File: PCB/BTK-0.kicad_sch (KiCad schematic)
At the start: 94 parts, among them J1 USB_C_Receptacle_USB2.0_16P, J2 BAT+, J3 BAT-, J4 Conn_01x15, J5 Conn_01x15_Socket, SW1 EN, SW10 1,2, SW11 2,2, SW12 3,2, SW13 4,2, SW14 5,2, SW15 6,2, SW16 1,3, SW17 2,3, SW18 3,3, SW19 4,3, SW2 BOOT, SW20 5,3, SW21 6,3, SW22 1,4, SW23 2,4, SW24 3,4, SW25 4,4, SW26 5,4, SW27 6,4, SW28 1,4, SW29 2,4, SW3 RotaryEncoder_Switch_MP, SW30 3,4, SW31 4,4, SW32 5,4, SW33 6,4, SW4 1,1, SW5 2,1, SW6 3,1, SW7 4,1, SW8 5,1, SW9 6,1, U1 NCP1117-3.3_SOT223, U2 NCP1117-3.3_SOT223, U3 USBLC6-2SC6, U4 ESP32-C6-MINI-1, U5 TVS1400DRV

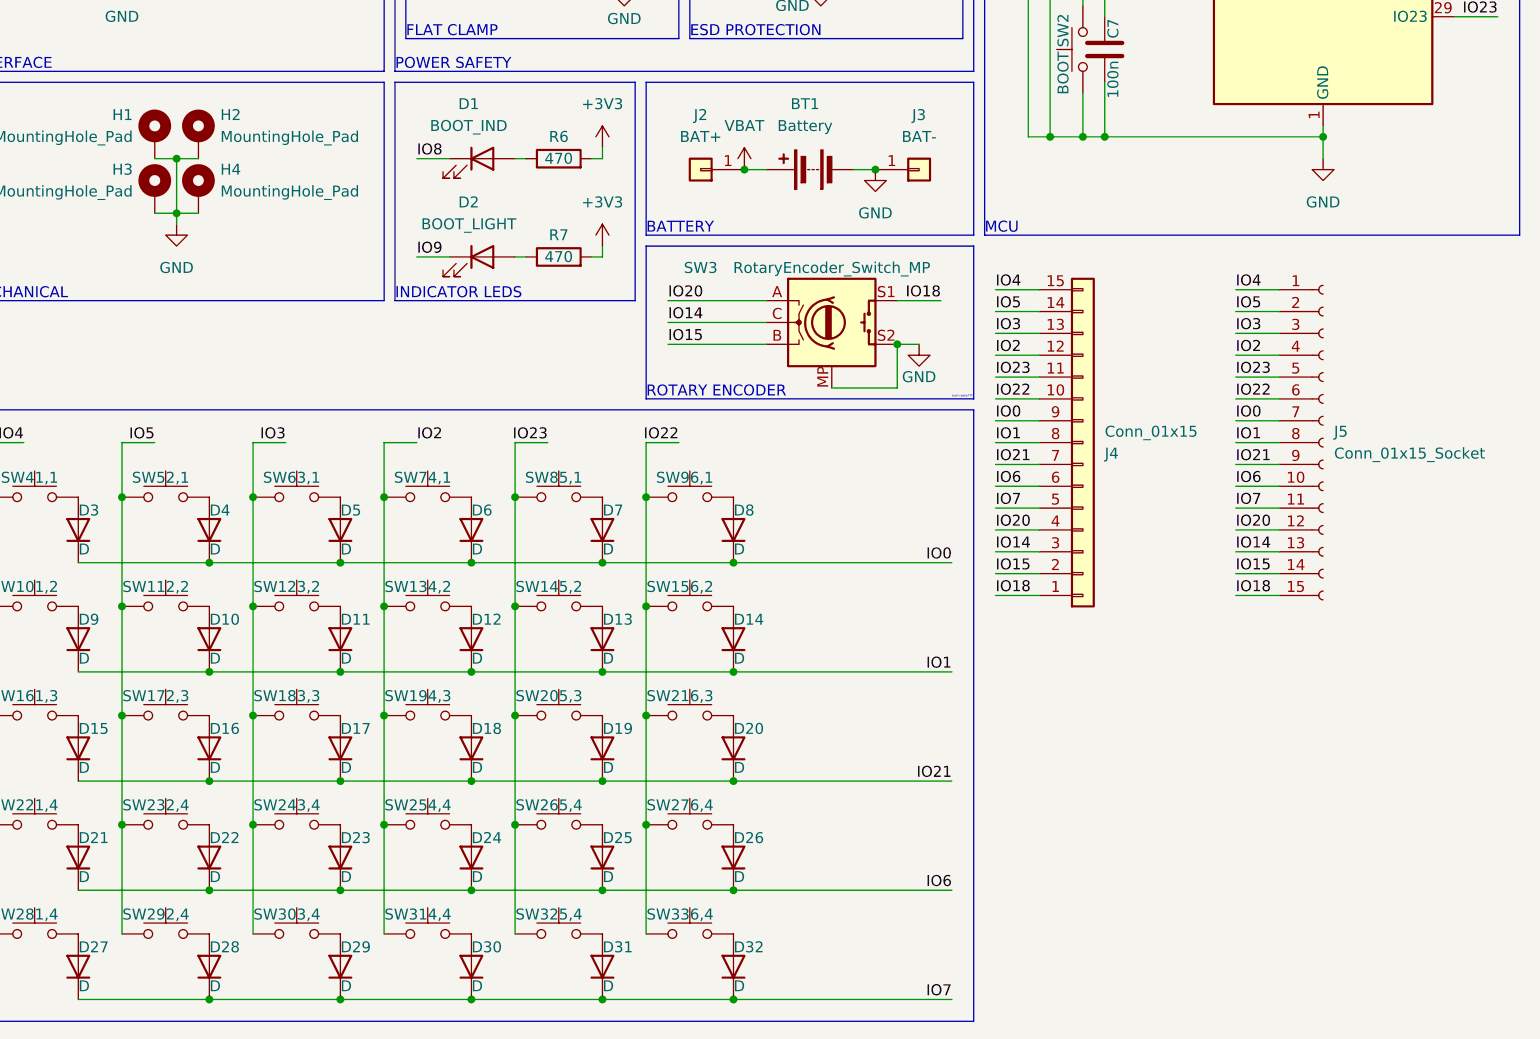
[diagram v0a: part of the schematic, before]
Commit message: fixed naming + control board more symmetrical, mcu to pin remap + mounting hole on control board
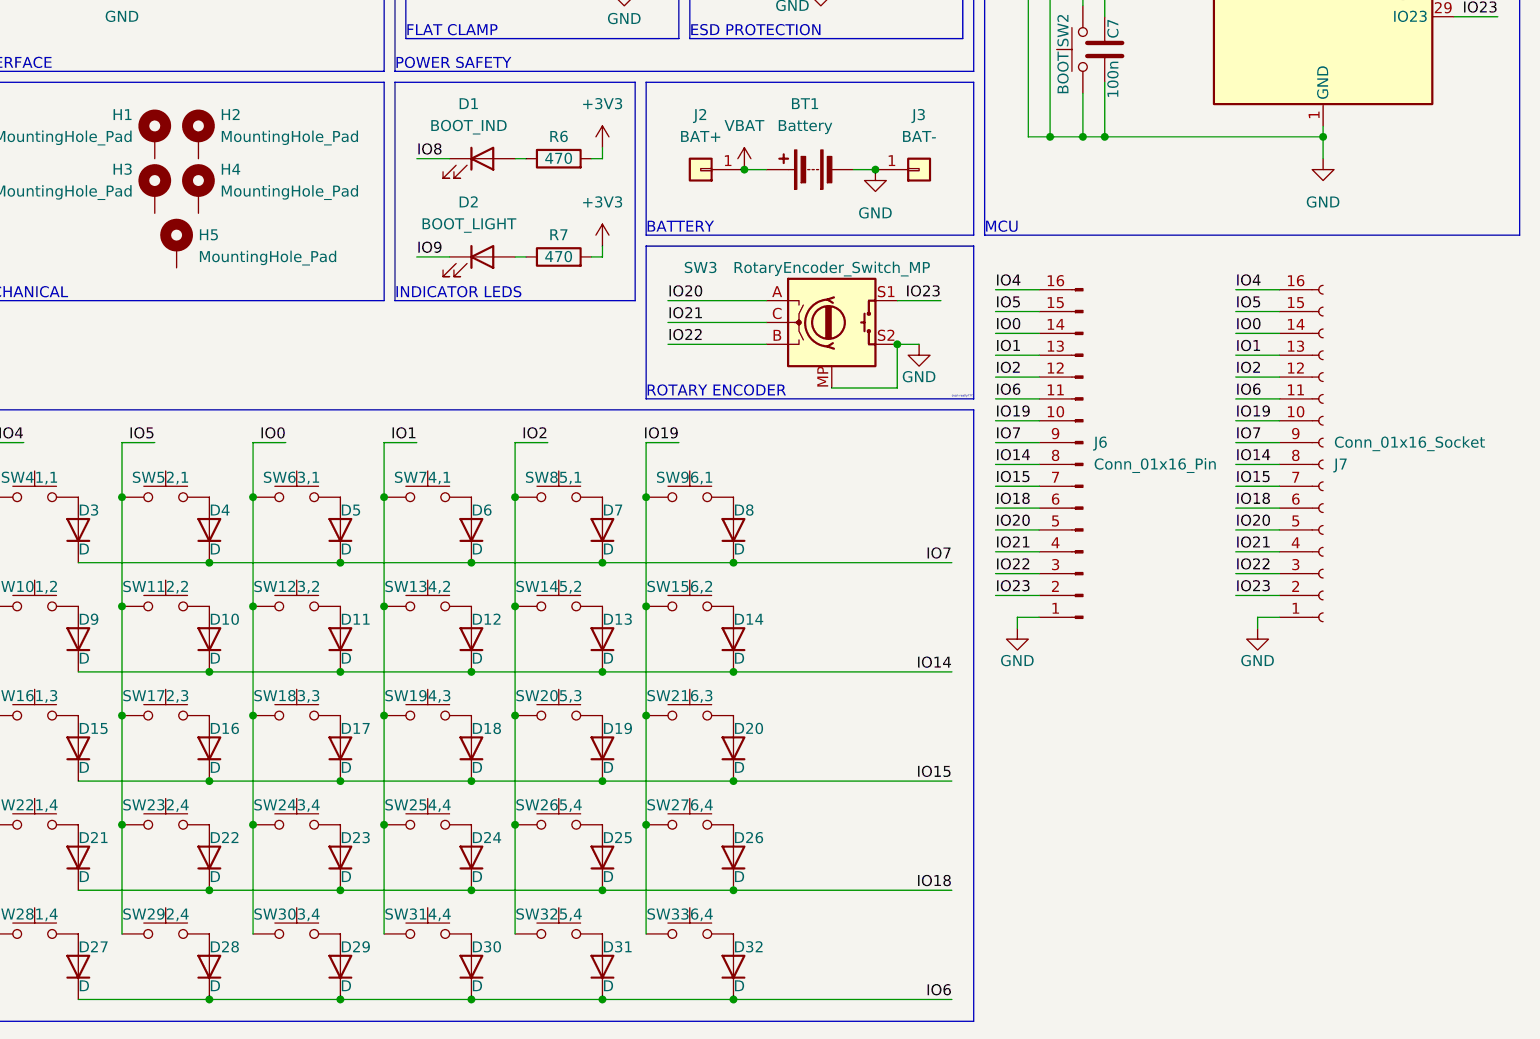
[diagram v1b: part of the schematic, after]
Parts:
- removed J4: Conn_01x15, Connector_PinHeader_1.00mm:PinHeader_1x15_P1.00mm_Horizontal, symbol Connector_Generic:Conn_01x15
- removed J5: Conn_01x15_Socket, Connector_PinSocket_1.00mm:PinSocket_1x15_P1.00mm_Vertical, symbol Connector:Conn_01x15_Socket
- added H5: MountingHole_Pad, MountingHole:MountingHole_3.2mm_M3_ISO7380, symbol Mechanical:MountingHole_Pad
- added J6: Conn_01x16_Pin, Connector_PinHeader_1.00mm:PinHeader_1x16_P1.00mm_Vertical, symbol Connector:Conn_01x16_Pin
- added J7: Conn_01x16_Socket, Connector_PinHeader_1.00mm:PinHeader_1x16_P1.00mm_Vertical, symbol Connector:Conn_01x16_Socket
- H1, H2, H3, H4: footprint MountingHole:MountingHole_3.2mm_M3 -> MountingHole:MountingHole_3.2mm_M3_ISO7380
- SW1, SW2: footprint Button_Switch_SMD:SW_Push_SPST_NO_Alps_SKRK -> Button_Switch_THT:SW_PUSH_1P1T_6x3.5mm_H4.3_APEM_MJTP1243
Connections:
- net GND: now also J6.1 (Pin_1), J7.1 (Pin_1); no longer H1.1, H2.1, H3.1, H4.1
- net IO0: now also SW12.1, SW18.1, SW24.1, SW30.1, SW6.1, J6.14 (Pin_14), J7.14 (Pin_14); no longer D3.1 (K), D4.1 (K), D5.1 (K), D6.1 (K), D7.1 (K), D8.1 (K)
- net IO1: now also SW13.1, SW19.1, SW25.1, SW31.1, SW7.1, J6.13 (Pin_13), J7.13 (Pin_13); no longer D10.1 (K), D11.1 (K), D12.1 (K), D13.1 (K), D14.1 (K), D9.1 (K)
- net IO14: now also D10.1 (K), D11.1 (K), D12.1 (K), D13.1 (K), D14.1 (K), D9.1 (K), J6.8 (Pin_8), J7.8 (Pin_8); no longer SW3.C
- net IO15: now also D15.1 (K), D16.1 (K), D17.1 (K), D18.1 (K), D19.1 (K), D20.1 (K), J6.7 (Pin_7), J7.7 (Pin_7); no longer SW3.B
- net IO18: now also D21.1 (K), D22.1 (K), D23.1 (K), D24.1 (K), D25.1 (K), D26.1 (K), J6.6 (Pin_6), J7.6 (Pin_6); no longer SW3.S1
- net IO19: now also SW15.1, SW21.1, SW27.1, SW33.1, SW9.1, J6.10 (Pin_10), J7.10 (Pin_10)
- net IO2: now also SW14.1, SW20.1, SW26.1, SW32.1, SW8.1, J6.12 (Pin_12), J7.12 (Pin_12); no longer SW13.1, SW19.1, SW25.1, SW31.1, SW7.1
- net IO20: now also J6.5 (Pin_5), J7.5 (Pin_5)
- net IO21: now also SW3.C, J6.4 (Pin_4), J7.4 (Pin_4); no longer D15.1 (K), D16.1 (K), D17.1 (K), D18.1 (K), D19.1 (K), D20.1 (K)
- net IO22: now also SW3.B, J6.3 (Pin_3), J7.3 (Pin_3); no longer SW15.1, SW21.1, SW27.1, SW33.1, SW9.1
- net IO23: now also SW3.S1, J6.2 (Pin_2), J7.2 (Pin_2); no longer SW14.1, SW20.1, SW26.1, SW32.1, SW8.1
- net IO3: no longer SW12.1, SW18.1, SW24.1, SW30.1, SW6.1
- net IO4: now also J6.16 (Pin_16), J7.16 (Pin_16)
- net IO5: now also J6.15 (Pin_15), J7.15 (Pin_15)
- net IO6: now also D27.1 (K), D28.1 (K), D29.1 (K), D30.1 (K), D31.1 (K), D32.1 (K), J6.11 (Pin_11), J7.11 (Pin_11); no longer D21.1 (K), D22.1 (K), D23.1 (K), D24.1 (K), D25.1 (K), D26.1 (K)
- net IO7: now also D3.1 (K), D4.1 (K), D5.1 (K), D6.1 (K), D7.1 (K), D8.1 (K), J6.9 (Pin_9), J7.9 (Pin_9); no longer D27.1 (K), D28.1 (K), D29.1 (K), D30.1 (K), D31.1 (K), D32.1 (K)

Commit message: fixing god knows what
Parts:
- D1, D2: footprint Diode_SMD:D_0805_2012Metric -> LED_SMD:LED_0805_2012Metric
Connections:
- net IO14: now also D3.1 (K), D4.1 (K), D5.1 (K), D6.1 (K), D7.1 (K), D8.1 (K), J6.9 (Pin_9), J7.9 (Pin_9); no longer D10.1 (K), D11.1 (K), D12.1 (K), D13.1 (K), D14.1 (K), D9.1 (K), J6.8 (Pin_8), J7.8 (Pin_8)
- net IO15: now also D10.1 (K), D11.1 (K), D12.1 (K), D13.1 (K), D14.1 (K), D9.1 (K), J6.8 (Pin_8), J7.8 (Pin_8); no longer D15.1 (K), D16.1 (K), D17.1 (K), D18.1 (K), D19.1 (K), D20.1 (K), J6.7 (Pin_7), J7.7 (Pin_7)
- net IO18: now also D15.1 (K), D16.1 (K), D17.1 (K), D18.1 (K), D19.1 (K), D20.1 (K), J6.7 (Pin_7), J7.7 (Pin_7); no longer D21.1 (K), D22.1 (K), D23.1 (K), D24.1 (K), D25.1 (K), D26.1 (K), J6.6 (Pin_6), J7.6 (Pin_6)
- net IO19: now also D21.1 (K), D22.1 (K), D23.1 (K), D24.1 (K), D25.1 (K), D26.1 (K), J6.6 (Pin_6), J7.6 (Pin_6); no longer J6.10 (Pin_10), J7.10 (Pin_10), SW15.1, SW21.1, SW27.1, SW33.1, SW9.1
- net IO7: now also J6.10 (Pin_10), J7.10 (Pin_10), SW15.1, SW21.1, SW27.1, SW33.1, SW9.1; no longer D3.1 (K), D4.1 (K), D5.1 (K), D6.1 (K), D7.1 (K), D8.1 (K), J6.9 (Pin_9), J7.9 (Pin_9)

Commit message: im boutta die son
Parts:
- added C10, C11, C8, C9: 4.7u, Capacitor_SMD:C_0402_1005Metric, symbol Device:C
- added D33, D34: LED, LED_SMD:LED_0805_2012Metric, symbol Device:LED
- added H6: MountingHole_Pad, MountingHole:MountingHole_3.2mm_M3_ISO7380, symbol Mechanical:MountingHole_Pad
- added R10: 4.7k, Resistor_SMD:R_0402_1005Metric, symbol Device:R
- added R11: 10k, Resistor_SMD:R_0402_1005Metric, symbol Device:R
- added R12, R13, R9: 1k, Resistor_SMD:R_0402_1005Metric, symbol Device:R
- added R8: 27k, Resistor_SMD:R_0402_1005Metric, symbol Device:R
- added U6: BQ24075RGT, Package_DFN_QFN:VQFN-16-1EP_3x3mm_P0.5mm_EP1.6x1.6mm, symbol Battery_Management:BQ24075RGT
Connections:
- net GND: now also C10.2, C11.2, C8.2, C9.2, R10.2, R11.2, R8.1, R9.1, U6.15 (SYSOFF), U6.17 (VSS), U6.4 (~{CE}), U6.6 (EN1), U6.8 (VSS)
- net VBAT: now also C11.1, U6.2 (BAT), U6.3 (BAT)
- net VBUS: now also C8.1, U6.13 (IN), U6.5 (EN2); no longer C1.1, U1.3 (VI)
- new net: R11.1, U6.1 (TS)
- new net: R9.2, U6.12 (ILIM)
- new net: R8.2, U6.14 (TMR)
- new net: R10.1, U6.16 (ISET)
- new net: D34.1 (K), U6.7 (~{PGOOD})
- new net: D33.1 (K), U6.9 (~{CHG})
- new net: D33.2 (A), R13.1
- new net: D34.2 (A), R12.2
- new net VCC: C1.1, C10.1, C9.1, R12.1, R13.2, U1.3 (VI), U6.10 (OUT), U6.11 (OUT)
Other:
- moved on the sheet: D10, D11, D12, D13, D14, D15, D16, D17, D18, D19, D20, D21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

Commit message: restart
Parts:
- removed BT1: Battery, Connector_PinHeader_2.54mm:PinHeader_1x02_P2.54mm_Horizontal, symbol Device:Battery
- removed J2: BAT+, Connector_PinHeader_2.54mm:PinHeader_1x01_P2.54mm_Vertical, symbol Connector_Generic:Conn_01x01
- removed J3: BAT-, Connector_PinHeader_2.54mm:PinHeader_1x01_P2.54mm_Vertical, symbol Connector_Generic:Conn_01x01
- added J2: Battery, Connector_PinHeader_2.54mm:PinHeader_1x02_P2.54mm_Horizontal, symbol Connector_Generic:Conn_01x02
- R1, R2, R3, R4, R5, R6, R7: footprint Resistor_SMD:R_0603_1608Metric -> Resistor_SMD:R_0805_2012Metric
- R10, R11, R12, R13, R8: footprint Resistor_SMD:R_0402_1005Metric -> Resistor_SMD:R_0805_2012Metric
- R9: value 1k -> 1.5k; footprint Resistor_SMD:R_0402_1005Metric -> Resistor_SMD:R_0805_2012Metric
- SW10, SW11, SW12, SW13, SW14, SW15, SW16, SW17, SW18, SW19, SW20, SW21, SW22, SW23, SW24, SW25, SW26, SW27, SW28, SW29, SW30, SW31, SW32, SW33, SW4, SW5, SW6, SW7, SW8, SW9: footprint KB_SWITCH:SW_MX_reversible -> kb_switch:SW_MX_reversible
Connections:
- net GND: now also J2.2 (Pin_2)
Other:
- note added: "BMS"
- note added: "IO BRIDGE"
- note added: "SWITCHES"
- moved on the sheet: C10, C11, C8, C9, D10, D11, D12, D13, D14, D15, D16, D17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

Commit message: we're so back
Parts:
- added R14: 10k, Resistor_SMD:R_0805_2012Metric, symbol Device:R
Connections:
- net GND: now also R14.1; no longer U6.15 (SYSOFF)
- net VBAT: now also J2.1 (Pin_1)
- net VBUS: no longer U6.5 (EN2)
- net VCC: now also U6.5 (EN2)
- new net: R14.2, U6.15 (SYSOFF)
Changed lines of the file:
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@@
 	(wire
 		(pts
-			(xy 120.65 82.55) (xy 120.65 85.09)
-		)
-		(stroke
-			(width 0)
-			(type default)
-		)
-	)
-	(wire
-		(pts
 			(xy 58.42 151.13) (xy 59.69 151.13)
 		)
@@
 	(wire
 		(pts
+			(xy 31.75 130.81) (xy 33.02 130.81)
+		)
+		(stroke
+			(width 0)
+			(type default)
+		)
+	)
+	(wire
+		(pts
 			(xy 111.76 49.53) (xy 111.76 50.8)
 		)
@@
 	(wire
 		(pts
-			(xy 33.02 130.81) (xy 21.59 130.81)
-		)
-		(stroke
-			(width 0)
-			(type default)
-		)
-	)
-	(wire
-		(pts
 			(xy 39.37 113.03) (xy 45.72 113.03)
 		)
@@
 	(wire
 		(pts
+			(xy 21.59 130.81) (xy 24.13 130.81)
+		)
+		(stroke
+			(width 0)
+			(type default)
+		)
+	)
+	(wire
+		(pts
 			(xy 91.44 22.86) (xy 87.63 22.86)
 		)
@@
 	(wire
 		(pts
-			(xy 17.78 113.03) (xy 17.78 143.51)
+			(xy 17.78 111.76) (xy 17.78 143.51)
 		)
 		(stroke
@@
 	(wire
 		(pts
+			(xy 120.65 82.55) (xy 120.65 85.09)
+		)
+		(stroke
+			(width 0)
+			(type default)
+		)
+	)
+	(wire
+		(pts
 			(xy 86.36 85.09) (xy 85.09 85.09)
 		)
@@
 	)
 	(symbol
+		(lib_id "Device:R")
+		(at 27.94 130.81 90)
+		(unit 1)
+		(body_style 1)
+		(exclude_from_sim no)
+		(in_bom yes)
+		(on_board yes)
+		(in_pos_files yes)
+		(dnp no)
+		(property "Reference" "R14"
+			(at 27.94 128.905 90)
+			(show_name no)
+			(do_not_autoplace no)
+			(effects
+				(font
+					(size 1.27 1.27)
+				)
+			)
+		)
+		(property "Value" "10k"
+			(at 27.94 130.81 90)
+			(show_name no)
+			(do_not_autoplace no)
+			(effects
+				(font
+					(size 1.27 1.27)
+				)
+			)
+		)
+		(property "Footprint" "Resistor_SMD:R_0805_2012Metric"
+			(at 27.94 132.588 90)
+			(hide yes)
+			(show_name no)
+			(do_not_autoplace no)
+			(effects
+				(font
+					(size 1.27 1.27)
+				)
+			)
+		)
+		(property "Datasheet" ""
+			(at 27.94 130.81 0)
+			(hide yes)
+			(show_name no)
+			(do_not_autoplace no)
+			(effects
+				(font
+					(size 1.27 1.27)
+				)
+			)
+		)
+		(property "Description" "Resistor"
+			(at 27.94 130.81 0)
+			(hide yes)
+			(show_name no)
+			(do_not_autoplace no)
+			(effects
+				(font
+					(size 1.27 1.27)
+				)
+			)
+		)
+		(pin "2"
+		)
+		(pin "1"
+		)
+		(instances
+			(project "BTK-0"
+				(path "/a809c93c-d7d1-4001-af5c-24ca3b5c5d40"
+					(reference "R14")
+					(unit 1)
+				)
+			)
+		)
+	)
+	(symbol
 		(lib_id "Device:LED")
 		(at 72.39 96.52 0)
@@
 	(symbol
 		(lib_id "power:VBUS")
-		(at 17.78 113.03 0)
+		(at 17.78 111.76 0)
 		(unit 1)
 		(body_style 1)
@@
 		(in_pos_files yes)
 		(dnp no)
-		(fields_autoplaced yes)
 		(property "Reference" "#PWR030"
-			(at 17.78 116.84 0)
+			(at 17.78 115.57 0)
 			(hide yes)
 			(show_name no)
@@
 			)
 		)
-		(property "Value" "VBUS"
-			(at 17.78 107.95 0)
+		(property "Value" "VCC"
+			(at 17.78 106.68 0)
 			(show_name no)
 			(do_not_autoplace no)
@@
 		)
 		(property "Footprint" ""
-			(at 17.78 113.03 0)
+			(at 17.78 111.76 0)
 			(hide yes)
 			(show_name no)
@@
 		)
 		(property "Datasheet" ""
-			(at 17.78 113.03 0)
+			(at 17.78 111.76 0)
 			(hide yes)
 			(show_name no)
@@
 		)
 		(property "Description" "Power symbol creates a global label with name \"VBUS\""
-			(at 17.78 113.03 0)
+			(at 17.78 111.76 0)
 			(hide yes)
 			(show_name no)
@@
 	(symbol
 		(lib_id "power:VDDF")
-		(at 120.6431 82.55 0)
+		(at 120.65 82.55 0)
 		(unit 1)
 		(body_style 1)
@@
 		(dnp no)
 		(property "Reference" "#PWR018"
-			(at 120.6431 86.36 0)
+			(at 120.65 86.36 0)
 			(hide yes)
 			(show_name no)
@@
 		)
 		(property "Value" "VBAT"
-			(at 120.65 78.74 0)
+			(at 120.6569 78.74 0)
 			(show_name no)
 			(do_not_autoplace no)
@@
 		)
 		(property "Footprint" ""
-			(at 120.6431 82.55 0)
+			(at 120.65 82.55 0)
 			(hide yes)
 			(show_name no)
@@
 		)
 		(property "Datasheet" ""
-			(at 120.6431 82.55 0)
+			(at 120.65 82.55 0)
 			(hide yes)
 			(show_name no)
@@
 		)
 		(property "Description" "Power symbol creates a global label with name \"VDDF\""
-			(at 120.6431 82.55 0)
+			(at 120.65 82.55 0)
 			(hide yes)
 			(show_name no)

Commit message: final DRC fixes
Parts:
- added D5: TXRX_IND, LED_SMD:LED_0805_2012Metric, symbol Device:LED
- added R15: 470, Resistor_SMD:R_0805_2012Metric, symbol Device:R
- C10, C11, C8, C9: footprint Capacitor_SMD:C_0402_1005Metric -> Capacitor_SMD:C_0805_2012Metric
- D3: renamed from D1; value BOOT_IND -> MODE_IND
- D4: renamed from D2; value BOOT_LIGHT -> BOOT_IND
- J1: footprint Connector_USB:USB_C_Receptacle_GCT_USB4105-xx-A_16P_TopMnt_Horizontal -> USB4510_03_1_A:GCT_USB4510-03-1-A_REVA
- J2: footprint Connector_PinHeader_2.54mm:PinHeader_1x02_P2.54mm_Horizontal -> Connector_PinHeader_2.54mm:PinHeader_1x02_P2.54mm_Vertical
- renumbered D34 to D1, D7 to D10, D8 to D11, D9 to D12, D10 to D13, D11 to D14, D12 to D15, D13 to D16, D14 to D17, D15 to D18, D16 to D19, D33 to D2, D17 to D20, D18 to D21, D19 to D22, D20 to D23, D21 to D24, D22 to D25, D23 to D26, D24 to D27, D25 to D28, D26 to D29, D27 to D30, D28 to D31, D29 to D32, D30 to D33, D31 to D34, D32 to D35, D3 to D6, D4 to D7, D5 to D8, D6 to D9, J6 to J3, J7 to J4, R12 to R10, R10 to R11, R13 to R12, R6 to R13, R7 to R14, R14 to R6, R8 to R7, R11 to R8
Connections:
- net +3V3: now also R15.2
- net IO3: now also D5.1 (K)
- net VBAT: no longer C3.1, U2.3 (VI), U5.4 (IN), U5.5 (IN), U5.6 (IN)
- net VBUS: now also C1.1, U1.3 (VI), U5.4 (IN), U5.5 (IN), U5.6 (IN)
- net VCC: now also C3.1, U2.3 (VI); no longer C1.1, U1.3 (VI)
- new net: D5.2 (A), R15.1
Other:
- moved on the sheet: C10, C11, C8, C9, D1, D2, D3, D4, H1, H2, H3, H4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
